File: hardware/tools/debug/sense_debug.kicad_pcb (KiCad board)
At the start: 4 copper layers, 14.8 x 38.8 mm, 53 parts, among them J1 Conn_01x03_Pin, J2 Conn_01x20_Pin, J3 Conn_01x03_Pin, J4 Conn_01x15_Pin, J5 Conn_01x12_Pin, Q1 Si1308EDL, U1 TMP117AIDRVR, U2 NTAG link, U3 ATtiny1626-MFR

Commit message: preliminary placement for debug board
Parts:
- removed C22: SUPER/HYBRIDCAP, Capacitor_SMD:C_0603_1608Metric
- added J6: B2B-PH-SM4-TB_LF__SN_, unsurv_offline_pcb_footprints:solar_2conn_solder, F.Cu at (73.5, 54.0)
- J2, QR_ref1, TP1, TP2, TP3, TP4, TP5, TP6, TP7: moved to F.Cu
- R1, R2, R4, R5: footprint Resistor_SMD:R_0402_1005Metric -> Resistor_SMD:R_0603_1608Metric
- moved C21 110.9 mm to (73.2, 58.0)
- moved TP8 110.3 mm to (74.0, 62.0), turned to 180 degrees
- moved U4 110.0 mm to (73.5, 68.3), turned to 180 degrees
- moved C16 107.4 mm to (70.0, 74.0), turned to 180 degrees
- moved TP9 106.5 mm to (80.0, 58.5), turned to 180 degrees
- moved C15 103.9 mm to (73.2, 74.0), turned to 180 degrees
- moved C20 103.4 mm to (78.0, 64.7), turned to -90 degrees
- moved J4 101.3 mm to (86.0, 51.1), turned to 180 degrees
- moved C19 100.7 mm to (80.0, 64.7), turned to -90 degrees
- moved C14 100.5 mm to (76.5, 74.0), turned to 180 degrees
- moved C18 99.2 mm to (80.0, 68.2), turned to -90 degrees
- moved C17 98.1 mm to (80.0, 71.7), turned to -90 degrees
- moved J3 97.6 mm to (85.6, 87.0), turned to -90 degrees
- moved J1 81.4 mm to (97.4, 87.0), turned to 90 degrees
- moved D3 78.0 mm to (93.5, 62.4), turned to -90 degrees
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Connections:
- U2 pad 14: ANT1 -> ANT2
- U2 pad 15: ANT2 -> ANT1
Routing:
- net GND: track 30.1 -> 0.00 mm, vias 2 -> 0
- net SCL: track 20.9 -> 0.00 mm, vias 1 -> 0
- net SDA: track 12.6 -> 0.00 mm, vias 1 -> 0
- net TX: track 10.5 -> 0.00 mm
- net VCC: track 7.12 -> 0.00 mm
- net RX: track 5.35 -> 0.00 mm
- net PS: track 4.35 -> 0.00 mm
- net ANT1: track 3.31 -> 0.00 mm, vias 1 -> 0
- net UPDI: track 0.83 -> 0.00 mm
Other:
- board size 14.8 x 38.8 mm -> 65 x 40 mm
- board text removed: "TX RX GND"
- board text removed: "VCC UPDI GND"
- board text removed: "v 0.1 Made in Germany 11/25"

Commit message: route debug board
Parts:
- added J7: Conn_01x03_Pin, Connector_PinHeader_2.54mm:PinHeader_1x03_P2.54mm_Vertical, F.Cu at (82.4, 87.0)
- moved TP5 57.9 mm to (69.5, 84.0)
- moved TP1 42.4 mm to (82.5, 81.5), turned to 90 degrees
- moved TP2 40.2 mm to (85.5, 81.5), turned to 90 degrees
- moved TP7 32.7 mm to (97.5, 82.5), turned to 90 degrees
- moved TP6 29.2 mm to (100.0, 82.5), turned to 90 degrees
- moved J5 27.6 mm to (112.2, 82.8), turned to 180 degrees
- moved TP3 18.2 mm to (108.5, 87.0), turned to 90 degrees
- moved TP4 17.7 mm to (111.5, 87.0), turned to 90 degrees
- moved R2 10.3 mm to (83.5, 69.8), turned to 0 degrees
- moved R1 8.34 mm to (83.5, 71.8), turned to 0 degrees
- moved J3 8.00 mm to (77.6, 87.0)
- moved U3 5.00 mm to (87.5, 70.5), turned to 180 degrees
- moved U2 2.50 mm to (74.4, 81.4)
- moved C8 2.18 mm to (86.7, 55.7)
- moved C1 2.09 mm to (75.6, 78.6)
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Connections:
- C11 pad 1: Net-(D2-A) -> Net-(D2-K)
- D2 pad 1: PREVGH -> Net-(D2-K)
- D2 pad 2: Net-(D2-A) -> PREVGH
- J5 pad 2: VLDO -> unconnected-(J5-Pin_2-Pad2)
- J5 pad 3: VIN -> unconnected-(J5-Pin_3-Pad3)
- L1 pad 2: Net-(D2-A) -> Net-(D2-K)
- Q1 pad 3: Net-(D2-A) -> Net-(D2-K)
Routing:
- net SCL: track 0.00 -> 115.1 mm, vias 0 -> 7
- net SDA: track 0.00 -> 104.8 mm, vias 0 -> 5
- net CS: track 0.00 -> 44.6 mm, vias 0 -> 4
- net SCLK: track 0.00 -> 41.4 mm, vias 0 -> 2
- net SDI: track 0.00 -> 40.8 mm, vias 0 -> 2
- net D/C: track 0.00 -> 39.6 mm, vias 0 -> 2
- net RES: track 0.00 -> 38.7 mm, vias 0 -> 2
- net BUSY: track 0.00 -> 38.2 mm, vias 0 -> 3
- net VLDO: track 0.00 -> 31.3 mm, vias 0 -> 1
- net PS: track 0.00 -> 30.8 mm, vias 0 -> 12
- net GDR: track 0.00 -> 28.1 mm, vias 0 -> 2
- net RESE: track 0.00 -> 23.6 mm, vias 0 -> 2
- net UPDI: track 0.00 -> 22.0 mm
- net ANT1: track 0.00 -> 21.2 mm, vias 0 -> 1
- net PART_INT: track 0.00 -> 21.0 mm, vias 0 -> 2
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- added copper zone on B.Cu, net GND
- added copper zone on F.Cu, net GND
- added copper zone on In2.Cu, net GND
- added copper zone on In1.Cu, net PS
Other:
- outline, holes or cut-outs redrawn

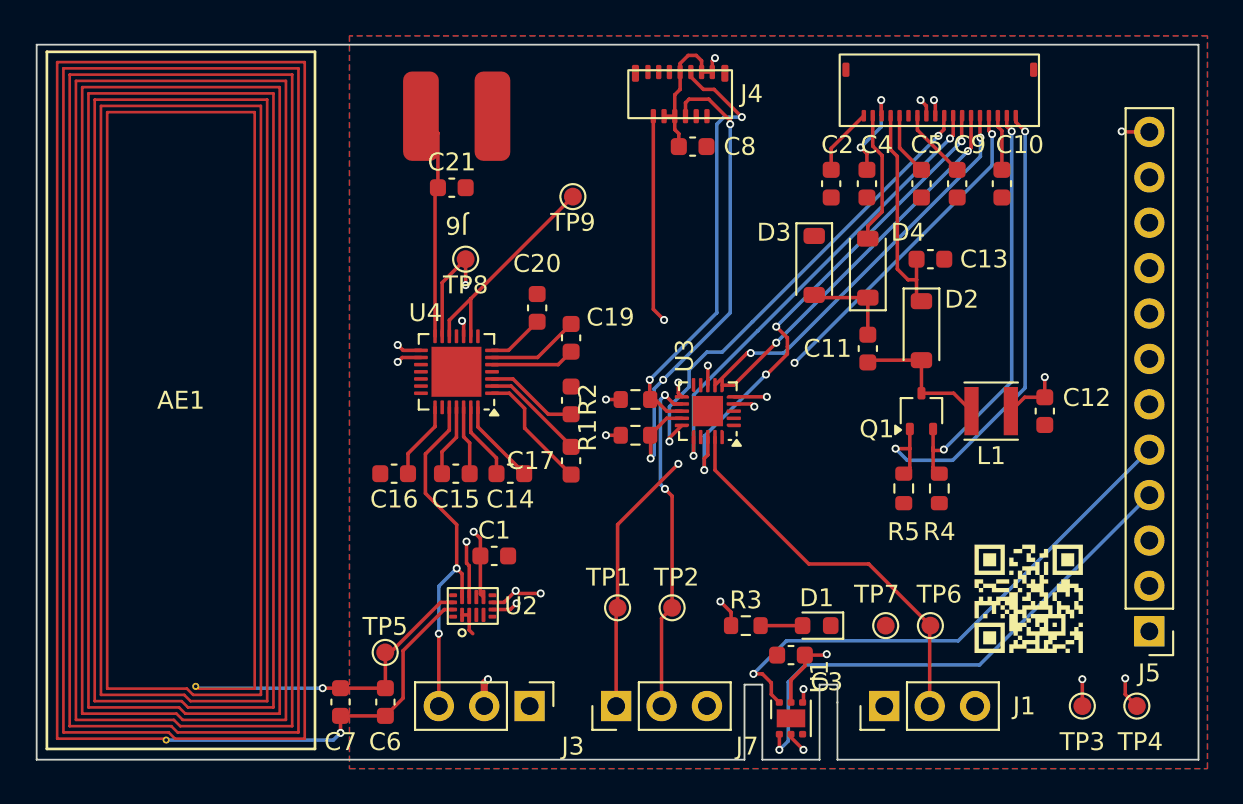
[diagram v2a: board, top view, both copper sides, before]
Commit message: new screen debug board
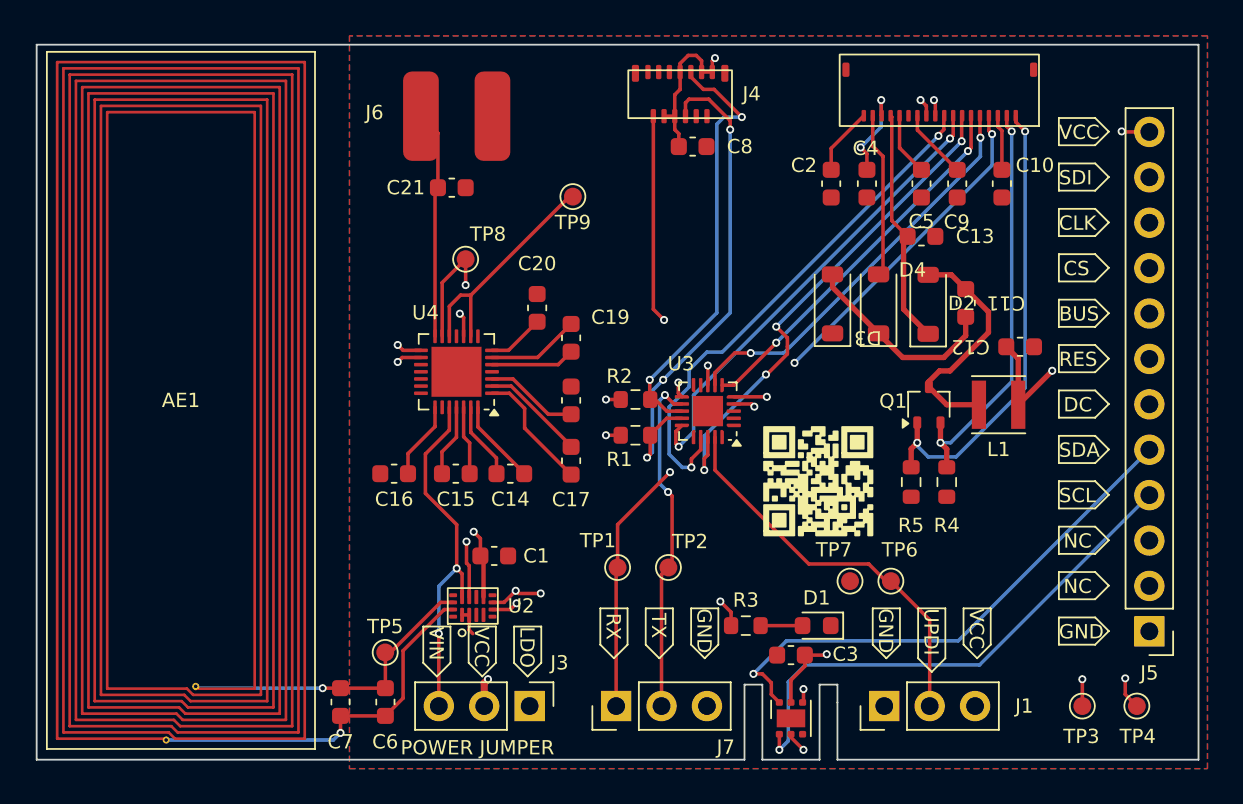
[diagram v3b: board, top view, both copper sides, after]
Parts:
- C13: value 1uF -> 4.7 uF
- moved QR_ref1 13.5 mm to (93.7, 74.4)
- moved C11 6.04 mm to (102.0, 64.5), turned to -90 degrees
- moved C12 3.86 mm to (105.0, 66.9), turned to 180 degrees
- moved TP6 3.33 mm to (97.8, 80.0)
- moved TP7 3.19 mm to (95.5, 80.0)
- moved D3 2.38 mm to (94.5, 64.5), turned to 90 degrees
- moved TP2 2.26 mm to (85.3, 79.2)
- moved TP1 2.25 mm to (82.5, 79.2)
- moved D4 2.09 mm to (97.1, 64.5)
- moved D2 1.52 mm to (99.9, 64.5), turned to 90 degrees
- moved C13 1.37 mm to (99.5, 60.7)
- moved Q1 0.55 mm to (99.9, 70.1)
- moved R4 0.55 mm to (100.9, 74.5)
- moved L1 0.55 mm to (103.8, 70.1)
- moved R5 0.55 mm to (98.9, 74.5)
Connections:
- C11 pad 1: Net-(D2-K) -> Net-(D2-A)
- D2 pad 1: Net-(D2-K) -> PREVGH
- D2 pad 2: PREVGH -> Net-(D2-A)
- L1 pad 2: Net-(D2-K) -> Net-(D2-A)
- Q1 pad 3: Net-(D2-K) -> Net-(D2-A)
- U3 pad 15: SDI -> SCLK
- U3 pad 16: SCLK -> SDO
- U3 pad 17: unconnected-(U3-PC2-Pad17) -> SDI
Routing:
- net Net-(D2-A): track 0.00 -> 13.4 mm
- net PREVGH: track 20.6 -> 13.3 mm
- net Net-(D3-A): track 5.14 -> 11.4 mm
- net SDI: track 40.8 -> 43.8 mm
- net PS: track 30.8 -> 33.7 mm
- net GDR: track 28.1 -> 26.1 mm
- net PREVGL: track 7.42 -> 9.22 mm
- net Net-(U4-LDOEN): track 12.8 -> 13.4 mm
- net RESE: track 23.6 -> 23.0 mm
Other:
- board text added: "BUS"
- board text added: "CLK"
- board text added: "CS"
- board text added: "DC"
- board text added: "GND"
- board text added: "LDO"
- board text added: "NC"
- board text added: "POWER JUMPER"
- board text added: "RES"
- board text added: "RX"
- board text added: "SCL"
- board text added: "SDA"
- board text added: "SDI"
- board text added: "TX"
- board text added: "UPDI"
- board text added: "VCC"
- board text added: "VIN"

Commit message: update SDO SDI SCLK
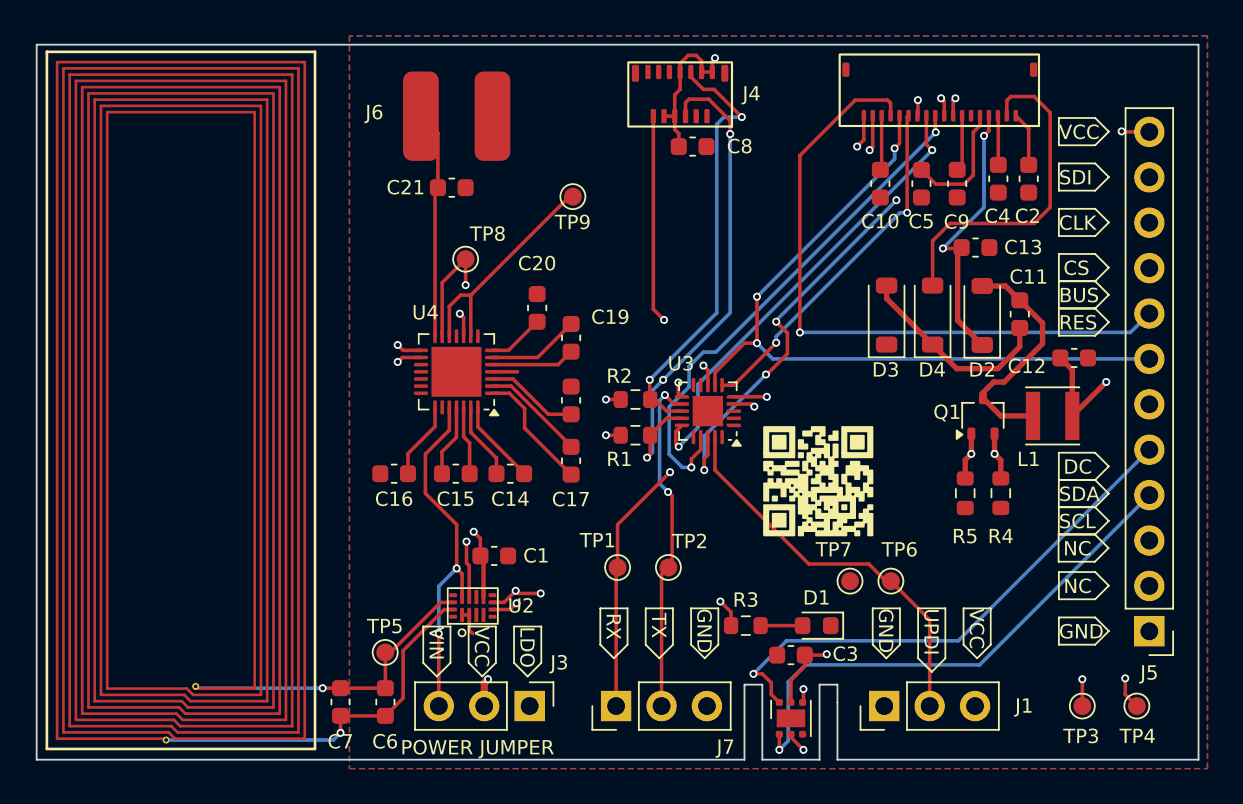
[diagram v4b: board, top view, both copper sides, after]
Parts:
- moved C2 11.1 mm to (105.5, 57.5)
- moved C4 7.36 mm to (103.8, 57.5)
- moved C10 6.80 mm to (97.2, 57.8)
- moved C11 3.09 mm to (105.0, 65.1)
- moved C12 3.09 mm to (108.0, 67.5)
- moved C13 3.09 mm to (102.5, 61.4)
- moved D2 3.09 mm to (102.9, 65.2)
- moved D4 3.09 mm to (100.1, 65.1)
- moved L1 3.09 mm to (106.8, 70.8)
- moved R5 3.09 mm to (102.0, 75.1)
- moved D3 3.09 mm to (97.5, 65.1)
- moved Q1 3.09 mm to (102.9, 70.8)
- moved R4 3.09 mm to (103.9, 75.1)
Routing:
- net PREVGL: track 9.22 -> 19.2 mm
- net BUSY: track 38.2 -> 44.4 mm, vias 3 -> 2
- net CS: track 44.6 -> 50.3 mm, vias 4 -> 5
- net Net-(J2-Pin_14): track 3.53 -> 6.92 mm
- net RESE: track 23.0 -> 26.3 mm
- net RES: track 39.1 -> 42.1 mm, vias 2 -> 3
- net Net-(J2-Pin_16): track 5.41 -> 2.76 mm, vias 2 -> 0
- net PREVGH: track 13.3 -> 15.7 mm, vias 0 -> 2
- net GND: track 13.9 -> 15.3 mm
- net D/C: track 39.6 -> 38.5 mm
- net SCLK: track 41.6 -> 42.5 mm
- net Net-(J2-Pin_12): track 3.95 -> 3.14 mm
- net Net-(J2-Pin_18): track 3.78 -> 3.05 mm
